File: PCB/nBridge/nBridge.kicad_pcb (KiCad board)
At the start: 2 copper layers, 30 x 30 mm, 21 parts, among them J1 USB_C_Receptacle_USB2.0, J2 Conn_01x06, J3 Conn_01x02, SW1 Switch-SPDT, U1 TPS7A0533PYKAR, U2 BQ25100YFPR, U3 BL652, U4 CC2500Module

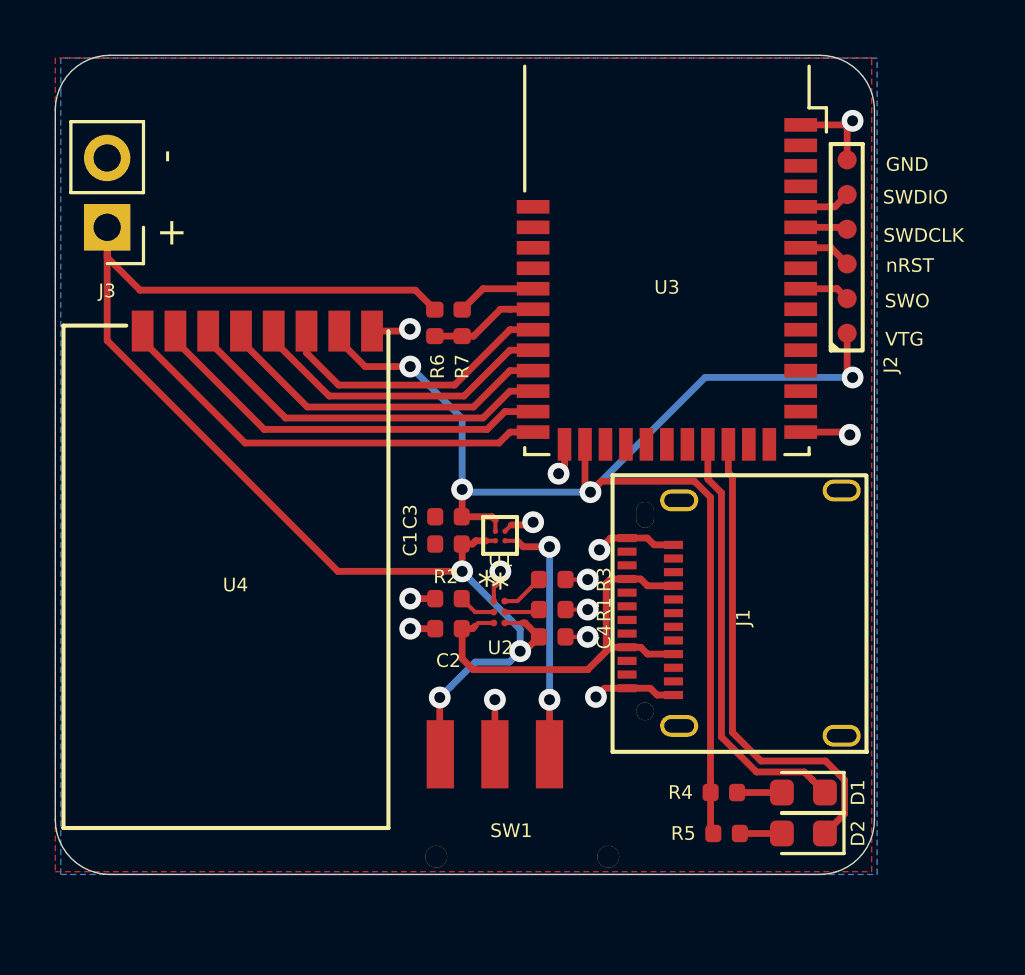
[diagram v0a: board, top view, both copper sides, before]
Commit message: Simplify design, fewer and more easily solderable components
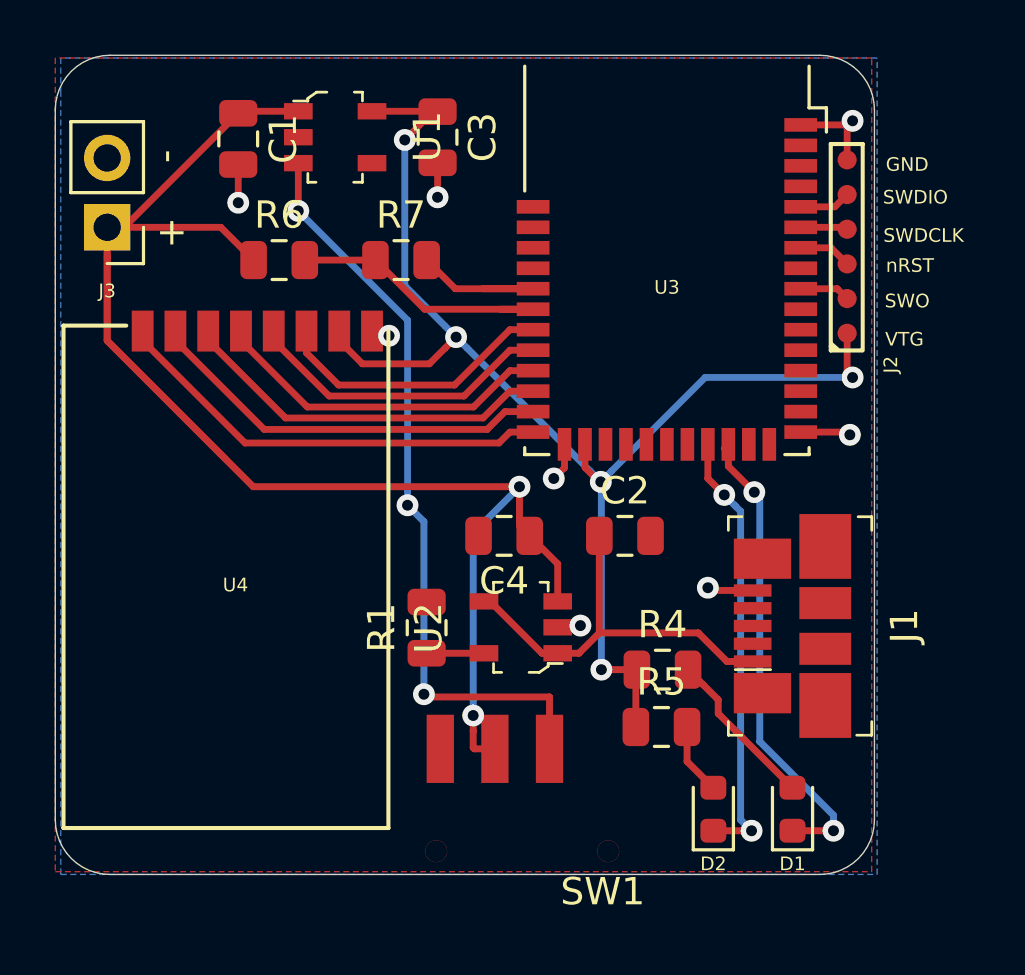
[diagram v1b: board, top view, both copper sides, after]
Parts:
- removed R2: 1k35, Resistor_SMD:R_0402_1005Metric
- removed R3: 6k, Resistor_SMD:R_0402_1005Metric
- C1, C2, C3, C4: footprint Capacitor_SMD:C_0402_1005Metric -> Capacitor_SMD:C_0805_2012Metric
- J1: value USB_C_Receptacle_USB2.0 -> 0473460001; footprint SharedFootprints:12401610E4#2A -> digikey-footprints:USB_Micro_B_Female_0473460001
- R1: value 10k -> R; footprint Resistor_SMD:R_0402_1005Metric -> Resistor_SMD:R_0805_2012Metric
- R4, R5, R6, R7: footprint Resistor_SMD:R_0402_1005Metric -> Resistor_SMD:R_0805_2012Metric
- U1: value TPS7A0533PYKAR -> LP5907MFX-3_3_NOPB; footprint SharedFootprints:TPS7A0533PYKAR -> digikey-footprints:SOT-753
- U2: value BQ25100YFPR -> MCP73812T-420I_OT; footprint SharedFootprints:BQ25100YFPR -> digikey-footprints:SOT-753
- moved C1 16.7 mm to (93.3, 122.3), turned to 270 degrees
- moved U1 15.8 mm to (96.8, 122.2), turned to 270 degrees
- moved C3 13.9 mm to (100.6, 122.2), turned to 270 degrees
- moved C2 7.30 mm to (107.5, 136.8), turned to 0 degrees
- moved R6 6.15 mm to (94.8, 126.7), turned to 0 degrees
- moved R4 5.03 mm to (108.8, 141.7)
- moved R1 4.65 mm to (100.2, 140.2), turned to 90 degrees
- moved R5 4.57 mm to (108.8, 143.8)
- moved C4 4.10 mm to (103.0, 136.8), turned to 180 degrees
- moved D2 3.42 mm to (110.7, 146.8), turned to 90 degrees
- moved R7 3.21 mm to (99.3, 126.7), turned to 0 degrees
- moved J1 3.13 mm to (114.8, 140.1), turned to 270 degrees
- moved U2 0.97 mm to (103.7, 140.2), turned to 90 degrees
- moved D1 0.73 mm to (113.6, 146.8), turned to 90 degrees
- moved SW1 0.20 mm to (100.7, 144.6)
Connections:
- C2 pad 1: Net-(C2-Pad1) -> /USB+
- D1 pad 1: /LED0 -> /LED1
- D2 pad 1: /LED1 -> /LED0
- SW1 pad 1: /V_BAT -> GND
- SW1 pad 2: GND -> /V_BAT
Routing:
- net Net-(SW1-Pad3): track 9.32 -> 28.9 mm, vias 2 -> 3
- net Net-(C2-Pad1): track 16.2 -> 0.00 mm
- net /USB+: track 0.00 -> 14.9 mm
- net /V_BAT: track 48.7 -> 62.2 mm, vias 3 -> 2
- net GND: track 22.8 -> 12.7 mm, vias 14 -> 8
- net /BAT_MSR: track 4.01 -> 10.3 mm
- net Net-(D1-Pad2): track 1.53 -> 5.91 mm
- net /BAT_MSR_EN: track 2.92 -> 6.17 mm
- net Net-(R3-Pad1): track 1.58 -> 0.00 mm
- net Net-(R2-Pad1): track 1.38 -> 0.00 mm
- net +3V3: track 48.1 -> 49.4 mm, vias 4 -> 5
- net Net-(D2-Pad2): track 1.53 -> 2.62 mm
- net Net-(R1-Pad1): track 1.29 -> 2.10 mm
- net /LED0: track 15.6 -> 16.2 mm, vias 0 -> 2
- net /LED1: track 17.7 -> 17.5 mm, vias 0 -> 2

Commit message: Minor modifications
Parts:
- moved C2 3.12 mm to (108.8, 139.6)
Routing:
- net /USB+: track 14.9 -> 12.0 mm
- net GND: track 12.7 -> 12.2 mm, vias 8 -> 9
- net Net-(SW1-Pad3): track 28.9 -> 29.1 mm, vias 3 -> 2
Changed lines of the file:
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@@
     (thickness 1.6)
     (drawings 19)
-    (tracks 188)
+    (tracks 189)
     (zones 0)
     (modules 19)
@@
   )
   (module Capacitor_SMD:C_0805_2012Metric (layer F.Cu)
-    (at 107.4625 136.8)
+    (at 108.8375 139.6)
     (descr "Capacitor SMD 0805 (2012 Metric), square (rectangular) end terminal, IPC_7351 nominal, (Body size source: https://docs.google.com/spreadsheets/d/1BsfQQcO9C6DZCsRaXUlFlo91Tg2WpOkGARC1WS5S8t0/edit?usp=sharing), generated with kicad-footprint-generator")
     (tags capacitor)
@@
   (segment (start 105 140.15) (end 105.768734 140.15) (width 0.152) (layer F.Cu) (net 2) (status 10))
   (segment (start 105.768734 140.15) (end 105.832361 140.086373) (width 0.152) (layer F.Cu) (net 2))
-  (via (at 110.5 138.7) (size 0.8) (drill 0.4) (layers F.Cu B.Cu) (net 2))
-  (segment (start 112.14 138.8) (end 110.6 138.8) (width 0.254) (layer F.Cu) (net 2) (status 10))
-  (segment (start 110.6 138.8) (end 110.5 138.7) (width 0.254) (layer F.Cu) (net 2))
+  (via (at 109 136.8) (size 0.8) (drill 0.4) (layers F.Cu B.Cu) (net 2))
+  (via (at 100.9 136.8) (size 0.8) (drill 0.4) (layers F.Cu B.Cu) (net 2))
+  (segment (start 102.1 136.8) (end 100.9 136.8) (width 0.254) (layer F.Cu) (net 2))
   (via (at 115.8 131) (size 0.8) (drill 0.4) (layers F.Cu B.Cu) (net 3))
   (segment (start 115.6 130.8) (end 115.8 131) (width 0.25) (layer F.Cu) (net 3))
@@
   (segment (start 104.7 144.6) (end 104.7 143.85) (width 0.25) (layer F.Cu) (net 26) (status 30))
   (segment (start 104.7 144.6) (end 104.7 144.351398) (width 0.25) (layer F.Cu) (net 26) (status 30))
-  (via (at 99.5 135.67901) (size 0.8) (drill 0.4) (layers F.Cu B.Cu) (net 26))
   (segment (start 95.5 124.9) (end 99.5 128.9) (width 0.25) (layer B.Cu) (net 26))
   (segment (start 99.5 135.113325) (end 99.5 135.67901) (width 0.25) (layer B.Cu) (net 26))
   (segment (start 99.5 128.9) (end 99.5 135.113325) (width 0.25) (layer B.Cu) (net 26))
+  (segment (start 99.22099 135.95802) (end 99.5 135.67901) (width 0.254) (layer F.Cu) (net 26))
+  (segment (start 99.22099 141.72099) (end 99.22099 135.95802) (width 0.254) (layer F.Cu) (net 26))
+  (segment (start 100.2 142.7) (end 99.22099 141.72099) (width 0.254) (layer F.Cu) (net 26))
+  (segment (start 104.7 142.7) (end 100.2 142.7) (width 0.254) (layer F.Cu) (net 26))
   (segment (start 104.7 144.6) (end 104.7 142.7) (width 0.254) (layer F.Cu) (net 26))
-  (segment (start 104.7 142.7) (end 100.2 142.7) (width 0.254) (layer F.Cu) (net 26))
-  (via (at 100.1 142.6) (size 0.8) (drill 0.4) (layers F.Cu B.Cu) (net 26))
-  (segment (start 100.2 142.7) (end 100.1 142.6) (width 0.254) (layer F.Cu) (net 26))
-  (segment (start 100.1 136.27901) (end 99.5 135.67901) (width 0.254) (layer B.Cu) (net 26))
-  (segment (start 100.1 142.6) (end 100.1 136.27901) (width 0.254) (layer B.Cu) (net 26))
+  (via (at 99.5 135.67901) (size 0.8) (drill 0.4) (layers F.Cu B.Cu) (net 26))
   (segment (start 115.01 126.25) (end 115.6 126.84) (width 0.25) (layer F.Cu) (net 27) (status 20))
   (segment (start 113.9 126.25) (end 115.01 126.25) (width 0.25) (layer F.Cu) (net 27) (status 10))
@@
   (segment (start 105.779 141.1) (end 105 141.1) (width 0.254) (layer F.Cu) (net 43) (status 20))
   (segment (start 106.525 140.354) (end 105.779 141.1) (width 0.254) (layer F.Cu) (net 43))
-  (segment (start 106.525 136.8) (end 106.525 140.354) (width 0.254) (layer F.Cu) (net 43) (status 10))
   (segment (start 104.425 141.1) (end 105 141.1) (width 0.254) (layer F.Cu) (net 43) (status 20))
   (segment (start 102.525 139.2) (end 104.425 141.1) (width 0.254) (layer F.Cu) (net 43) (status 10))
   (segment (start 102.3 139.2) (end 102.525 139.2) (width 0.254) (layer F.Cu) (net 43) (status 30))
-  (segment (start 110.15 140.354) (end 106.525 140.354) (width 0.254) (layer F.Cu) (net 43))
-  (segment (start 111.196 141.4) (end 110.15 140.354) (width 0.254) (layer F.Cu) (net 43))
-  (segment (start 112.14 141.4) (end 111.196 141.4) (width 0.254) (layer F.Cu) (net 43) (status 10))
+  (segment (start 107.146 140.354) (end 107.9 139.6) (width 0.254) (layer F.Cu) (net 43))
+  (segment (start 106.525 140.354) (end 107.146 140.354) (width 0.254) (layer F.Cu) (net 43))
+  (segment (start 111.196 141.4) (end 112.14 141.4) (width 0.254) (layer F.Cu) (net 43))
+  (segment (start 110.37501 140.57901) (end 111.196 141.4) (width 0.254) (layer F.Cu) (net 43))
+  (segment (start 108.87901 140.57901) (end 110.37501 140.57901) (width 0.254) (layer F.Cu) (net 43))
+  (segment (start 107.9 139.6) (end 108.87901 140.57901) (width 0.254) (layer F.Cu) (net 43))
   (zone (net 0) (net_name "") (layers F&B.Cu) (hatch edge 0.508)
     (connect_pads (clearance 0.508))

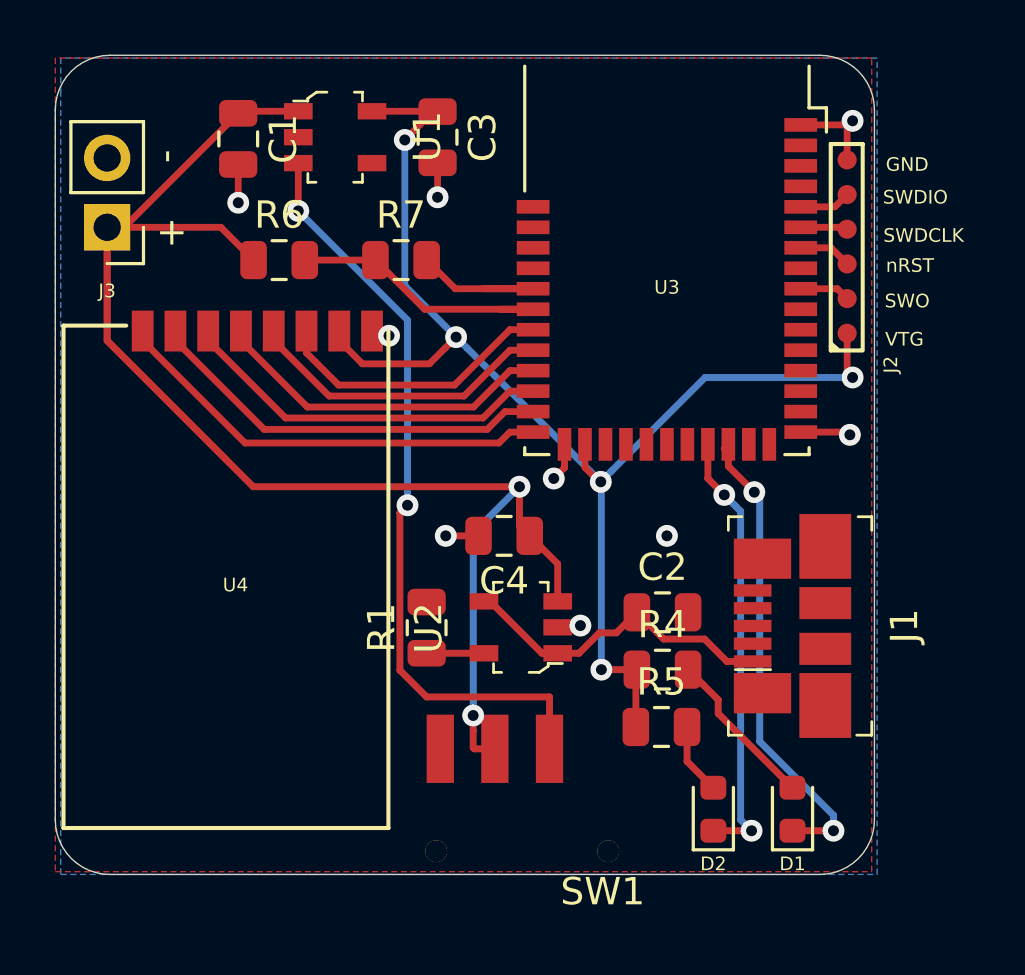
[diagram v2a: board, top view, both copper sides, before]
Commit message: Update part values and remove unused silkscreen
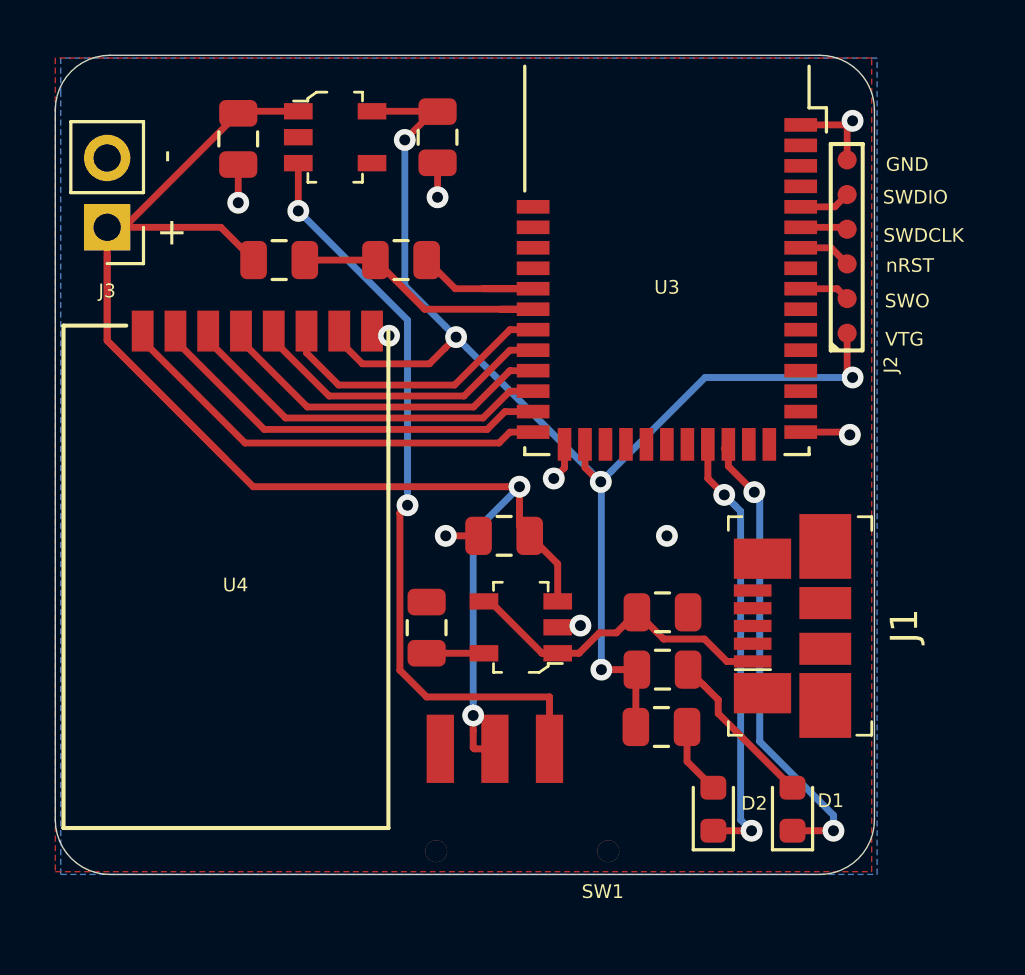
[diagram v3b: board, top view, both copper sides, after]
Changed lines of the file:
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@@
   (layers
     (0 F.Cu signal)
-    (31 B.Cu signal)
-    (32 B.Adhes user)
-    (33 F.Adhes user)
-    (34 B.Paste user)
-    (35 F.Paste user)
-    (36 B.SilkS user)
-    (37 F.SilkS user hide)
-    (38 B.Mask user)
-    (39 F.Mask user)
-    (40 Dwgs.User user)
-    (41 Cmts.User user)
-    (42 Eco1.User user)
-    (43 Eco2.User user)
-    (44 Edge.Cuts user)
-    (45 Margin user)
-    (46 B.CrtYd user)
-    (47 F.CrtYd user)
-    (48 B.Fab user)
+    (31 B.Cu signal hide)
+    (32 B.Adhes user hide)
+    (33 F.Adhes user hide)
+    (34 B.Paste user hide)
+    (35 F.Paste user hide)
+    (36 B.SilkS user hide)
+    (37 F.SilkS user)
+    (38 B.Mask user hide)
+    (39 F.Mask user hide)
+    (40 Dwgs.User user hide)
+    (41 Cmts.User user hide)
+    (42 Eco1.User user hide)
+    (43 Eco2.User user hide)
+    (44 Edge.Cuts user hide)
+    (45 Margin user hide)
+    (46 B.CrtYd user hide)
+    (47 F.CrtYd user hide)
+    (48 B.Fab user hide)
     (49 F.Fab user hide)
   )
@@
       (outputformat 1)
       (mirror false)
-      (drillshape 1)
+      (drillshape 0)
       (scaleselection 1)
       (outputdirectory ""))
@@
     (tags diode)
     (attr smd)
-    (fp_text reference D1 (at -2 0 180) (layer F.SilkS)
+    (fp_text reference D1 (at 0.3125 1.4 180) (layer F.SilkS)
       (effects (font (size 0.5 0.5) (thickness 0.125)))
     )
@@
     (tags diode)
     (attr smd)
-    (fp_text reference D2 (at -2 0) (layer F.SilkS)
+    (fp_text reference D2 (at 0.2125 1.5) (layer F.SilkS)
       (effects (font (size 0.5 0.5) (thickness 0.125)))
     )
@@
   (module digikey-footprints:SOT-753 (layer F.Cu)
     (at 96.85 122.2 270)
-    (fp_text reference U1 (at -0.025 -3.375 270) (layer F.SilkS)
+    (fp_text reference U1 (at -0.025 -3.375 270) (layer Cmts.User)
       (effects (font (size 1 1) (thickness 0.15)))
     )
@@
   (module digikey-footprints:SOT-753 (layer F.Cu)
     (at 103.65 140.15 90)
-    (fp_text reference U2 (at -0.025 -3.375 90) (layer F.SilkS)
+    (fp_text reference U2 (at 1.95 -2.35 180) (layer Cmts.User)
       (effects (font (size 1 1) (thickness 0.15)))
     )
@@
     (descr "Minor error in pad placement")
     (fp_text reference SW1 (at 5.95 5.23) (layer F.SilkS)
-      (effects (font (size 1 1) (thickness 0.15)))
+      (effects (font (size 0.5 0.5) (thickness 0.125)))
     )
     (fp_text value Switch-SPDT (at 3.31 2.28) (layer F.Fab)
@@
     (tags capacitor)
     (attr smd)
-    (fp_text reference C1 (at 0 -1.65 270) (layer F.SilkS)
+    (fp_text reference C1 (at 0 -1.65 270) (layer Cmts.User)
       (effects (font (size 1 1) (thickness 0.15)))
     )
@@
     (tags capacitor)
     (attr smd)
-    (fp_text reference C2 (at 0 -1.65) (layer F.SilkS)
+    (fp_text reference C2 (at 0 -1.65) (layer Cmts.User) hide
       (effects (font (size 1 1) (thickness 0.15)))
     )
@@
     (tags capacitor)
     (attr smd)
-    (fp_text reference C3 (at 0 -1.65 270) (layer F.SilkS)
+    (fp_text reference C3 (at 0 -1.65 270) (layer Cmts.User)
       (effects (font (size 1 1) (thickness 0.15)))
     )
@@
     (tags capacitor)
     (attr smd)
-    (fp_text reference C4 (at 0 -1.65 180) (layer F.SilkS)
+    (fp_text reference C4 (at 0 -1.65 180) (layer Cmts.User)
       (effects (font (size 1 1) (thickness 0.15)))
     )
@@
     (tags resistor)
     (attr smd)
-    (fp_text reference R1 (at 0 -1.65 90) (layer F.SilkS)
+    (fp_text reference R1 (at 0 -1.65 90) (layer Cmts.User)
       (effects (font (size 1 1) (thickness 0.15)))
     )
@@
     (tags resistor)
     (attr smd)
-    (fp_text reference R4 (at 0 -1.65) (layer F.SilkS)
+    (fp_text reference R4 (at 0 -1.65) (layer Cmts.User)
       (effects (font (size 1 1) (thickness 0.15)))
     )
@@
     (tags resistor)
     (attr smd)
-    (fp_text reference R5 (at 0 -1.65) (layer F.SilkS)
+    (fp_text reference R5 (at 0 -1.65) (layer Cmts.User)
       (effects (font (size 1 1) (thickness 0.15)))
     )
@@
     (tags resistor)
     (attr smd)
-    (fp_text reference R6 (at 0 -1.65) (layer F.SilkS)
+    (fp_text reference R6 (at 0 -1.65) (layer Cmts.User)
       (effects (font (size 1 1) (thickness 0.15)))
     )
@@
     (tags resistor)
     (attr smd)
-    (fp_text reference R7 (at 0 -1.65) (layer F.SilkS)
-      (effects (font (size 1 1) (thickness 0.15)))
-    )
+    (fp_text reference R7 (at 0 -1.65) (layer Cmts.User)
+      (effects (font (size 1 1) (thickness 0.15)))
+    )
